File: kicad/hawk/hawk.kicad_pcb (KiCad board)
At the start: 2 copper layers, 27.9 x 44.4 mm, 14 parts, among them J1 GPIO_AA, J2 GPIO_BB, J3 SWD_PGM, J4 Battery, SW1 SW_Push, U1 ATSAMD10C14A-SS, U2 AP7333-33SRG-7

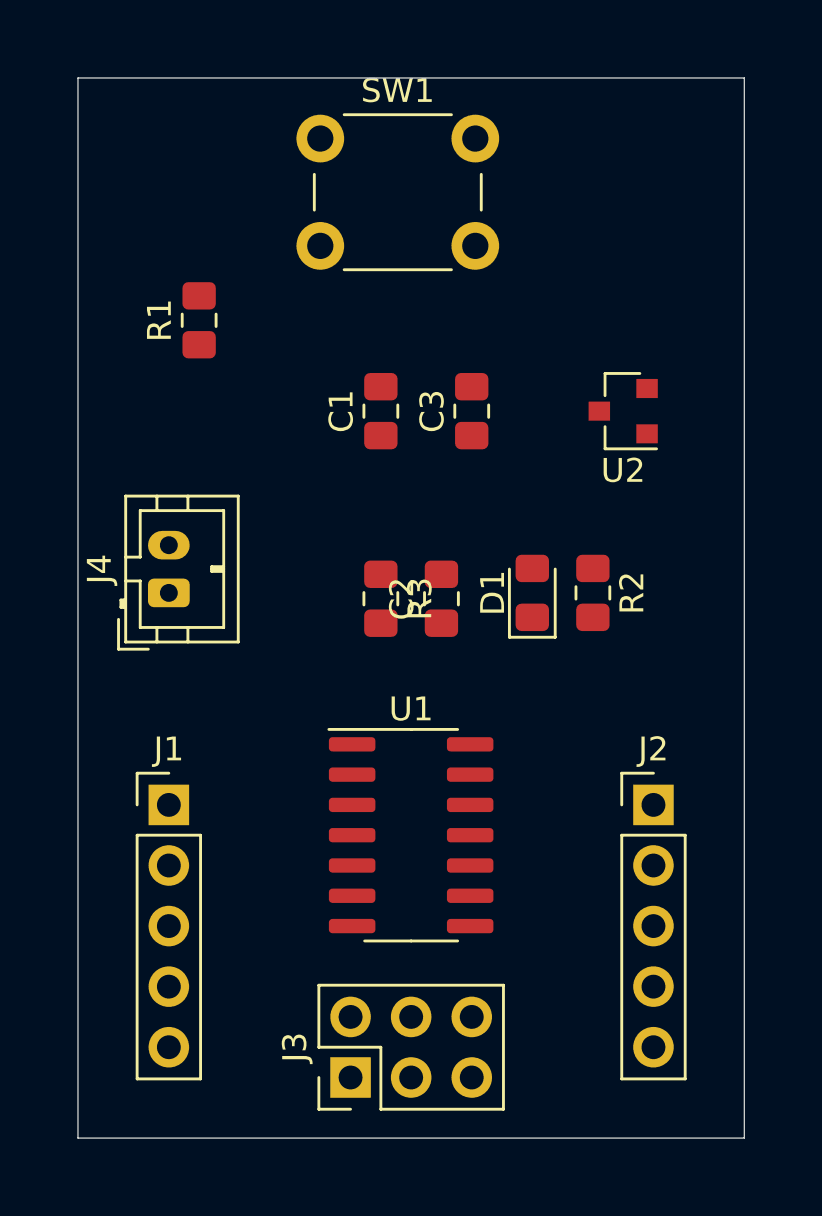
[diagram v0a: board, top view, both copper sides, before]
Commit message: [KICAD] Hawk tutorial pt. 5-8
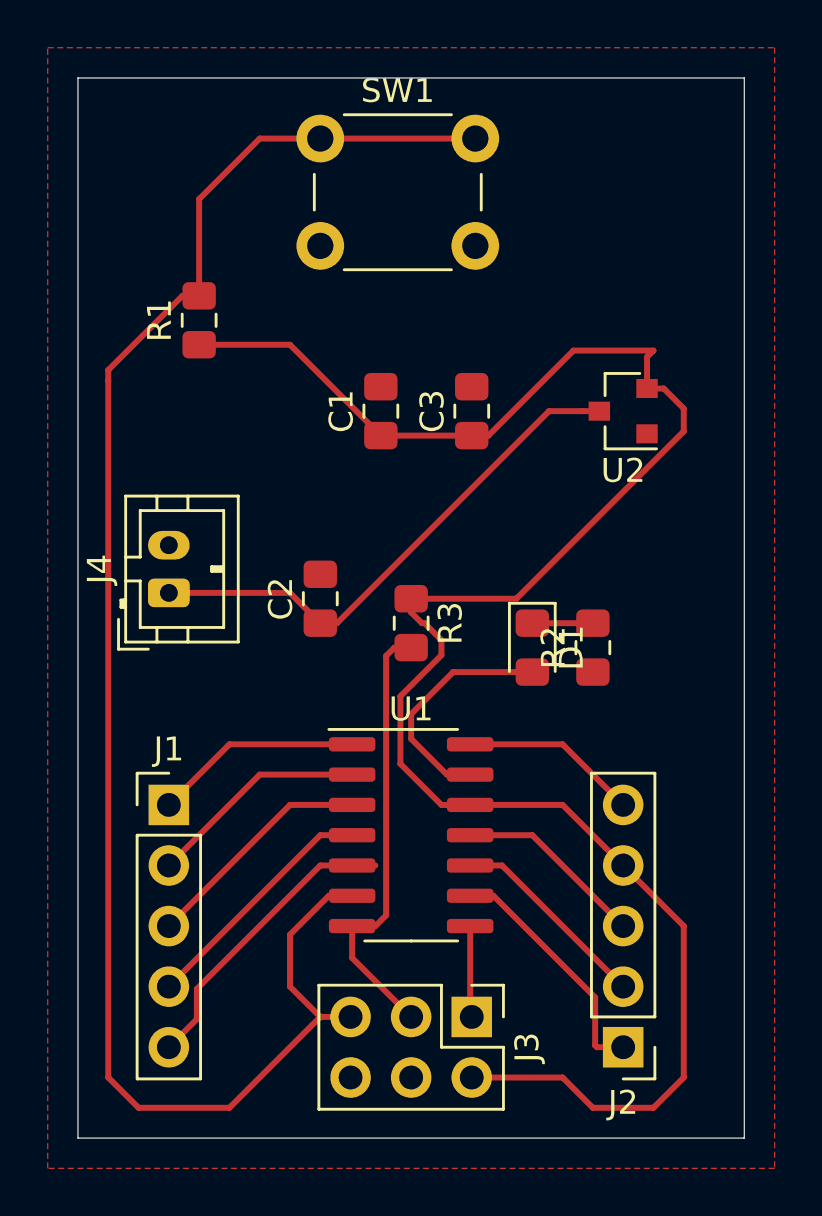
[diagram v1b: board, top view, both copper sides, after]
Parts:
- moved J2 10.2 mm to (144.8, 115.6), turned to 180 degrees
- moved J3 5.68 mm to (138.4, 114.3), turned to 270 degrees
- moved C2 5.08 mm to (132.1, 96.8)
- moved D1 2.30 mm to (141.0, 98.8), turned to 270 degrees
- moved R2 2.30 mm to (143.5, 98.8), turned to 90 degrees
- moved R3 1.63 mm to (135.9, 97.8)
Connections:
- J1 pad 1: +3V3 -> GPIO_4
- J1 pad 4: GPIO_3 -> GPIO_5
- J1 pad 5: GPIO_4 -> GPIO_6
- J2 pad 1: GND -> GPIO_7
- J2 pad 3: GPIO_7 -> GND
- J2 pad 4: GPIO_6 -> +3V3
- J2 pad 5: GPIO_5 -> GPIO_3
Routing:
- net +3V3: track 0.00 -> 80.2 mm
- net reset: track 0.00 -> 71.0 mm
- net +BATT: track 0.00 -> 22.3 mm
- net SWCLK: track 0.00 -> 18.8 mm
- net GPIO_6: track 0.00 -> 12.6 mm
- net GPIO_5: track 0.00 -> 10.3 mm
- net GPIO_7: track 0.00 -> 10.2 mm
- net LED: track 0.00 -> 9.95 mm
- net GPIO_2: track 0.00 -> 9.79 mm
- net GPIO_1: track 0.00 -> 9.26 mm
- net GPIO_4: track 0.00 -> 8.74 mm
- net GPIO_8: track 0.00 -> 8.52 mm
- net GND: track 0.00 -> 7.99 mm
- net GPIO_3: track 0.00 -> 7.47 mm
- net SWDIO: track 0.00 -> 3.84 mm
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- added copper zone on F.Cu, net GND

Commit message: [KICAD] Hawk tutorial pt. 9-End
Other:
- board text added: "HAWK PCB"
- board text added: "Mr. Paul"
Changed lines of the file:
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@@
   (general
     (thickness 1.6)
-    (drawings 4)
+    (drawings 6)
     (tracks 93)
     (zones 0)
@@
     (37 F.SilkS user)
     (38 B.Mask user)
-    (39 F.Mask user)
+    (39 F.Mask user hide)
     (40 Dwgs.User user)
     (41 Cmts.User user)
@@
     (tags "capacitor handsolder")
     (attr smd)
-    (fp_text reference C1 (at 0 -1.65 90) (layer F.SilkS)
+    (fp_text reference C1 (at 2.54 0 180) (layer F.SilkS)
       (effects (font (size 1 1) (thickness 0.15)))
     )
@@
     (tags "capacitor handsolder")
     (attr smd)
-    (fp_text reference C2 (at 0 -1.65 90) (layer F.SilkS)
+    (fp_text reference C2 (at 2.785 0 180) (layer F.SilkS)
       (effects (font (size 1 1) (thickness 0.15)))
     )
@@
     (tags "capacitor handsolder")
     (attr smd)
-    (fp_text reference C3 (at 0 -1.65 90) (layer F.SilkS)
+    (fp_text reference C3 (at 2.54 0 180) (layer F.SilkS)
       (effects (font (size 1 1) (thickness 0.15)))
     )
@@
     (tags "LED handsolder")
     (attr smd)
-    (fp_text reference D1 (at 0 -1.65 90) (layer F.SilkS)
+    (fp_text reference D1 (at 2.785 -2.54 180) (layer F.SilkS)
       (effects (font (size 1 1) (thickness 0.15)))
     )
@@
     (descr "Through hole straight pin header, 1x05, 2.54mm pitch, single row")
     (tags "Through hole pin header THT 1x05 2.54mm single row")
-    (fp_text reference J1 (at 0 -2.33) (layer F.SilkS)
+    (fp_text reference J1 (at 2.54 10.16) (layer F.SilkS)
       (effects (font (size 1 1) (thickness 0.15)))
     )
@@
     (descr "Through hole straight pin header, 1x05, 2.54mm pitch, single row")
     (tags "Through hole pin header THT 1x05 2.54mm single row")
-    (fp_text reference J2 (at 0 -2.33) (layer F.SilkS)
+    (fp_text reference J2 (at -2.54 10.16 180) (layer F.SilkS)
       (effects (font (size 1 1) (thickness 0.15)))
     )
@@
     (descr "Through hole straight pin header, 2x03, 2.54mm pitch, double rows")
     (tags "Through hole pin header THT 2x03 2.54mm double row")
-    (fp_text reference J3 (at 1.27 -2.33 90) (layer F.SilkS)
+    (fp_text reference J3 (at 0 -2.33 180) (layer F.SilkS)
       (effects (font (size 1 1) (thickness 0.15)))
     )
@@
     (descr "JST PH series connector, B2B-PH-K (http://www.jst-mfg.com/product/pdf/eng/ePH.pdf), generated with kicad-footprint-generator")
     (tags "connector JST PH side entry")
-    (fp_text reference J4 (at 1 -2.9 90) (layer F.SilkS)
+    (fp_text reference J4 (at -3.81 0 180) (layer F.SilkS)
       (effects (font (size 1 1) (thickness 0.15)))
     )
@@
     (tags "resistor handsolder")
     (attr smd)
-    (fp_text reference R1 (at 0 -1.65 90) (layer F.SilkS)
+    (fp_text reference R1 (at -2.54 0 180) (layer F.SilkS)
       (effects (font (size 1 1) (thickness 0.15)))
     )
@@
     (tags "resistor handsolder")
     (attr smd)
-    (fp_text reference R2 (at 0 -1.65 90) (layer F.SilkS)
+    (fp_text reference R2 (at -2.785 -2.54 180) (layer F.SilkS)
       (effects (font (size 1 1) (thickness 0.15)))
     )
@@
     (tags "resistor handsolder")
     (attr smd)
-    (fp_text reference R3 (at 0 -1.65 90) (layer F.SilkS)
+    (fp_text reference R3 (at -2.54 -1.27 180) (layer F.SilkS)
       (effects (font (size 1 1) (thickness 0.15)))
     )
@@
     (descr https://www.omron.com/ecb/products/pdf/en-b3f.pdf)
     (tags "tact sw push 6mm")
-    (fp_text reference SW1 (at 3.25 -2) (layer F.SilkS)
+    (fp_text reference SW1 (at -3.81 -1.27) (layer F.SilkS)
       (effects (font (size 1 1) (thickness 0.15)))
     )
@@
     (tags "SOIC SO")
     (attr smd)
-    (fp_text reference U1 (at 0 -5.28) (layer F.SilkS)
+    (fp_text reference U1 (at 0 5.08) (layer F.SilkS)
       (effects (font (size 1 1) (thickness 0.15)))
     )
@@
     (tags SOT-23)
     (attr smd)
-    (fp_text reference U2 (at 0 -2.5) (layer F.SilkS)
+    (fp_text reference U2 (at -1.27 3.81) (layer F.SilkS)
       (effects (font (size 1 1) (thickness 0.15)))
     )
@@
     )
   )
+  (gr_text "Mr. Paul" (at 144.78 77.47) (layer F.SilkS)
+    (effects (font (size 1 1) (thickness 0.15)))
+  )
+  (gr_text "HAWK PCB" (at 144.78 76.2) (layer F.SilkS)
+    (effects (font (size 1 1) (thickness 0.15)))
+  )
   (gr_line (start 121.92 119.38) (end 149.86 119.38) (layer Edge.Cuts) (width 0.05))
